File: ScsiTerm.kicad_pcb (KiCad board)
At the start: 2 copper layers, 36.1 x 23.4 mm, 25 parts, among them J1 DB25_Male, U1 LD1117DT28TR

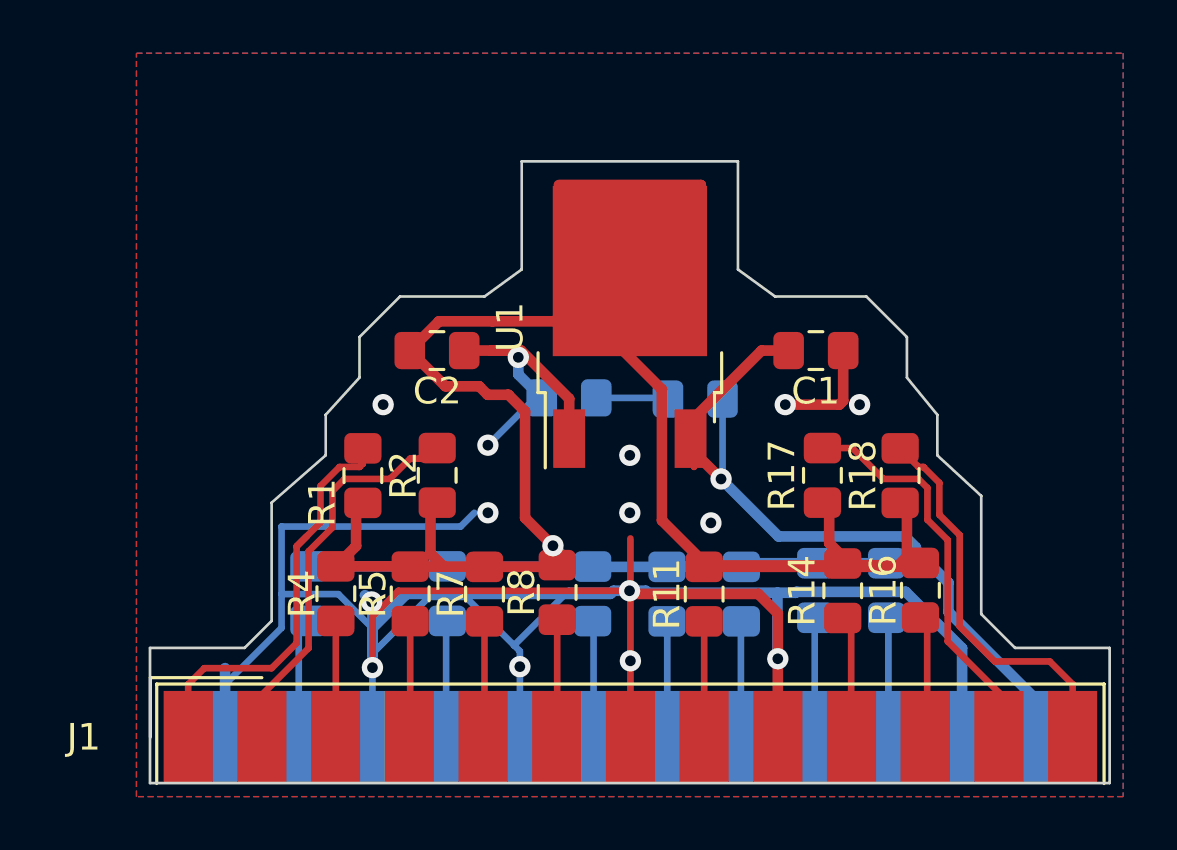
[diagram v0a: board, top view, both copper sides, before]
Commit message: Version 0.3: 2.85V regulator by adjustable variant This version will now use a more common voltage regulator since the 2.85V parts are going EOL.
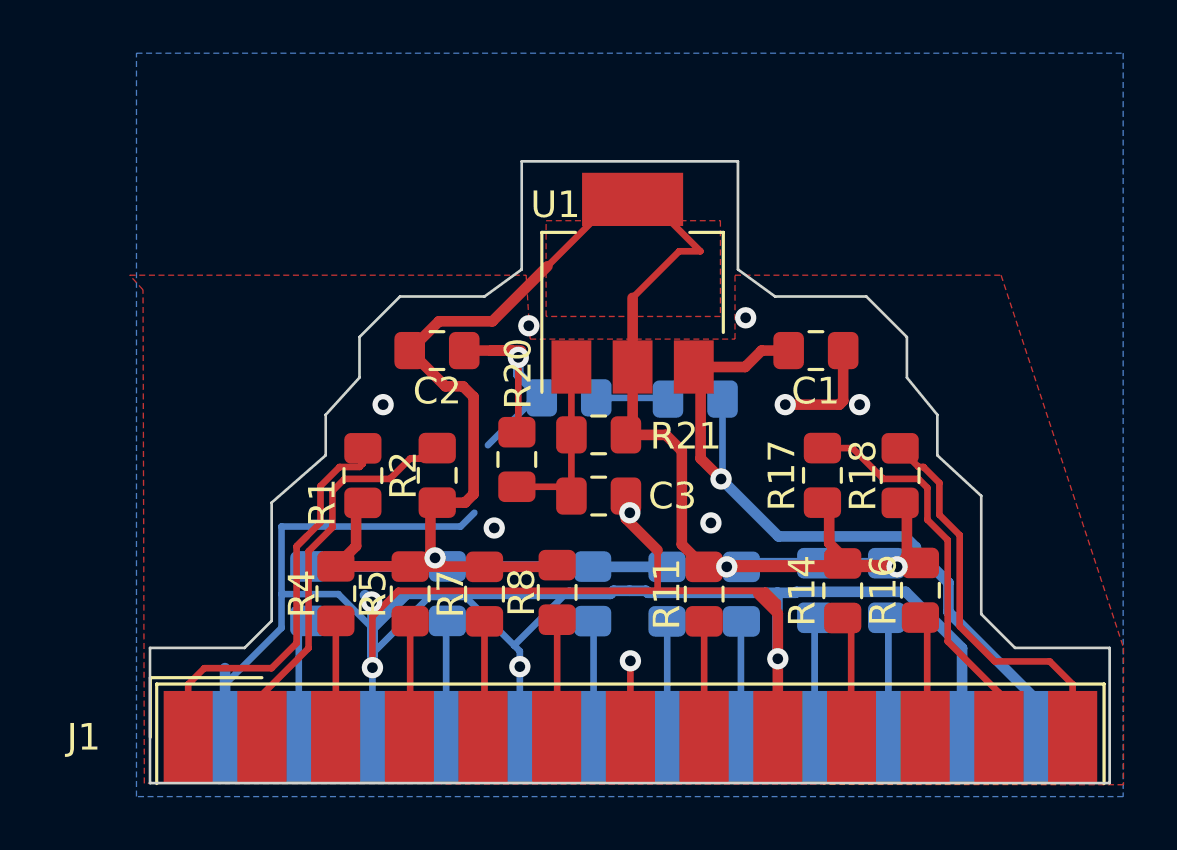
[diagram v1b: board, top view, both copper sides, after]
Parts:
- added C3: 4.7uF, Capacitor_SMD:C_0805_2012Metric_Pad1.15x1.40mm_HandSolder, F.Cu at (151.0, 58.3)
- added R20: 150, Resistor_SMD:R_0805_2012Metric_Pad1.15x1.40mm_HandSolder, F.Cu at (147.9, 56.9)
- added R21: 120, Resistor_SMD:R_0805_2012Metric_Pad1.15x1.40mm_HandSolder, F.Cu at (151.0, 56.0)
- U1: value LD1117DT28TR -> LD1117 SC-R; footprint Package_TO_SOT_SMD:TO-252-2 -> Package_TO_SOT_SMD:SOT-223-3_TabPin2
- moved U1 1.65 mm to (152.2, 50.3)
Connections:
- U1 pad 1: GND -> Net-(C3-Pad1)
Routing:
- net /2.85V: track 104.1 -> 96.3 mm, vias 1 -> 3
- net Net-(C3-Pad1): track 0.00 -> 7.19 mm
- net +5V: track 30.6 -> 28.9 mm
- net GND: track 121.1 -> 122.3 mm, vias 15 -> 14
- added copper zone on F.Cu, net /2.85V
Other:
- board text added: "©2022"
- board text removed: "©2021"
